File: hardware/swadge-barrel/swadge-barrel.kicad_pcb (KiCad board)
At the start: 2 copper layers, 70.4 x 89.6 mm, 46 parts, among them J1 USB_B_Micro, Q1 Q_NPN_BEC, SW1 SW_SPDT, U1 ESP-13-WROOM-02D, U2 OLED_DISPLAY, U3 BUS_PCIexpress, U4 QMA6981, U5 AP1117-33, U6 OLED_CONNECTOR

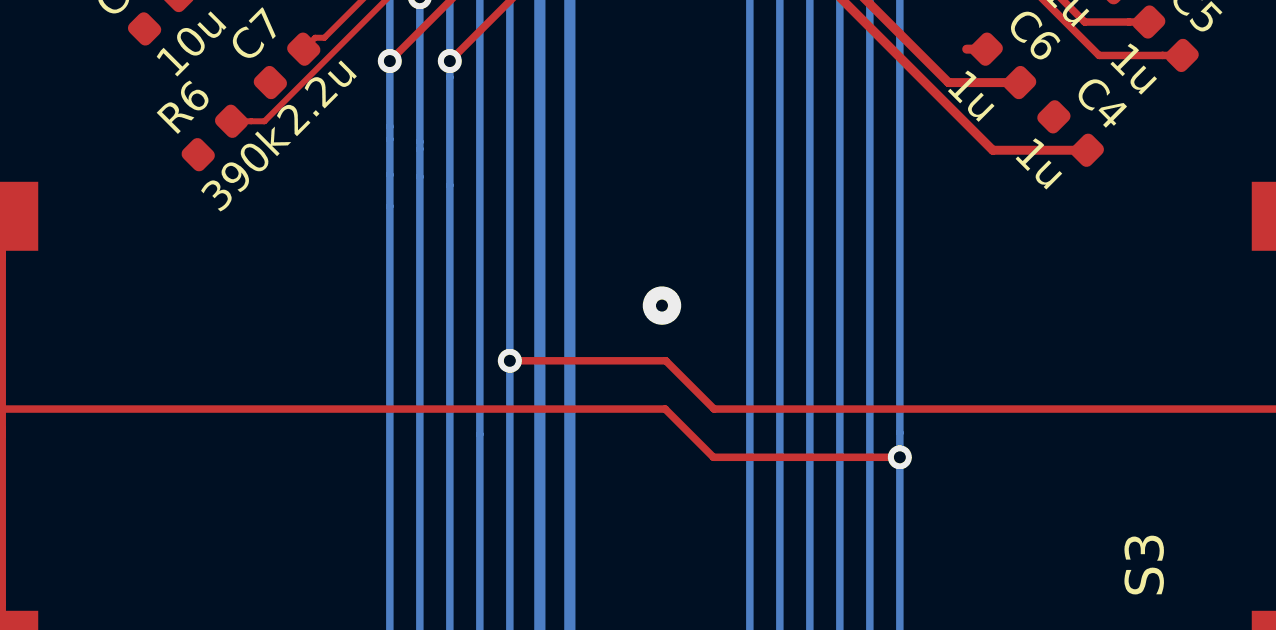
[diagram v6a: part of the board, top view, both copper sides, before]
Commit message: Added headband part and 3D model
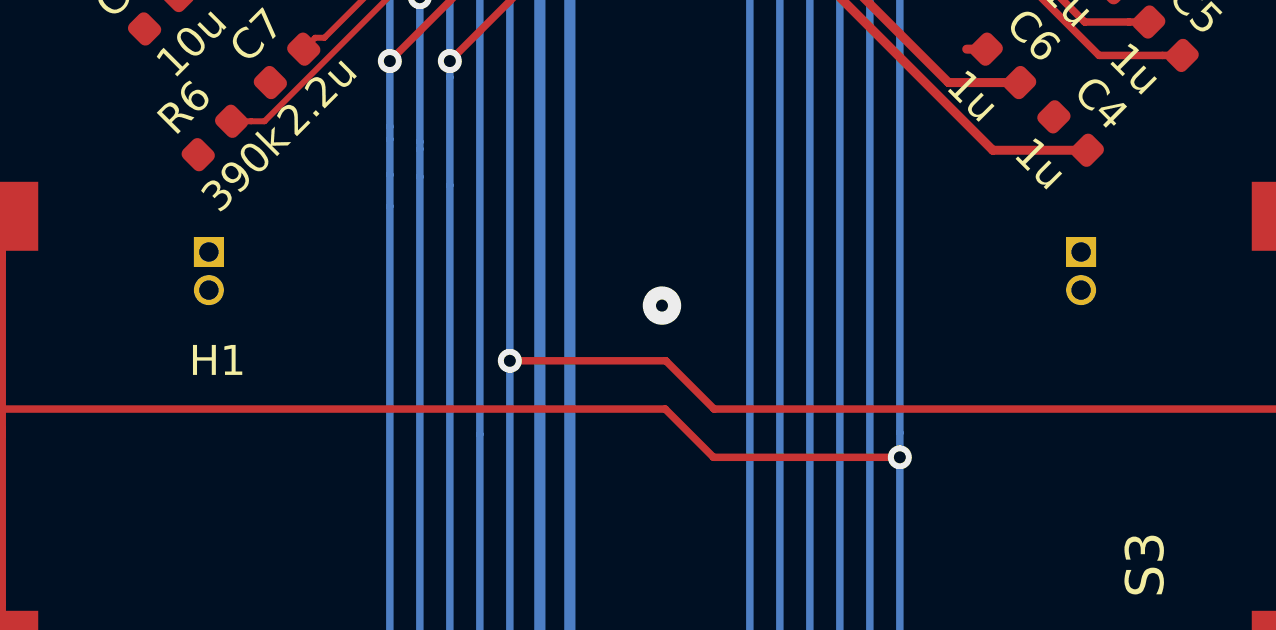
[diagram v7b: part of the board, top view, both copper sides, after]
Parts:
- added H1: Headband, Swadge_Parts:Headband, F.Cu at (145.5, 95.8)

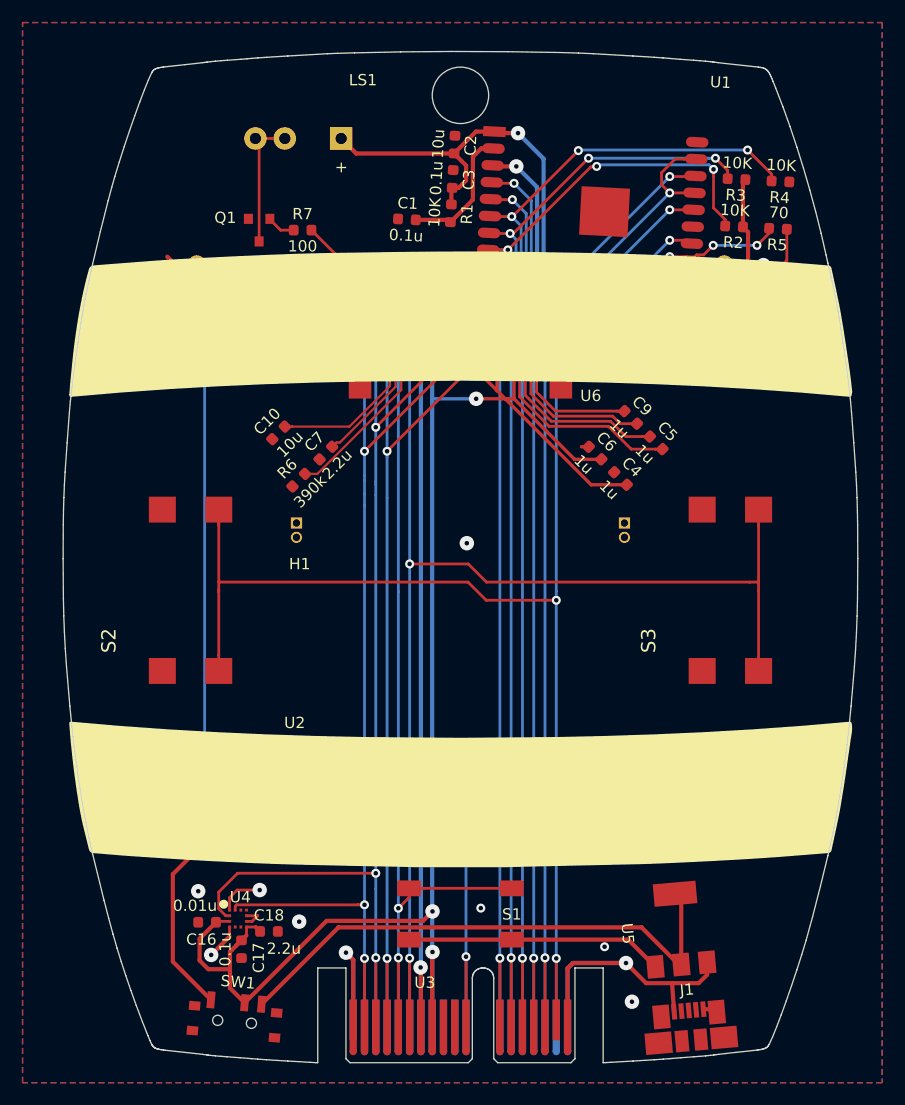
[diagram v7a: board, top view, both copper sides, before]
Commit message: Added vertical banding, shifted parts to avoid the bands
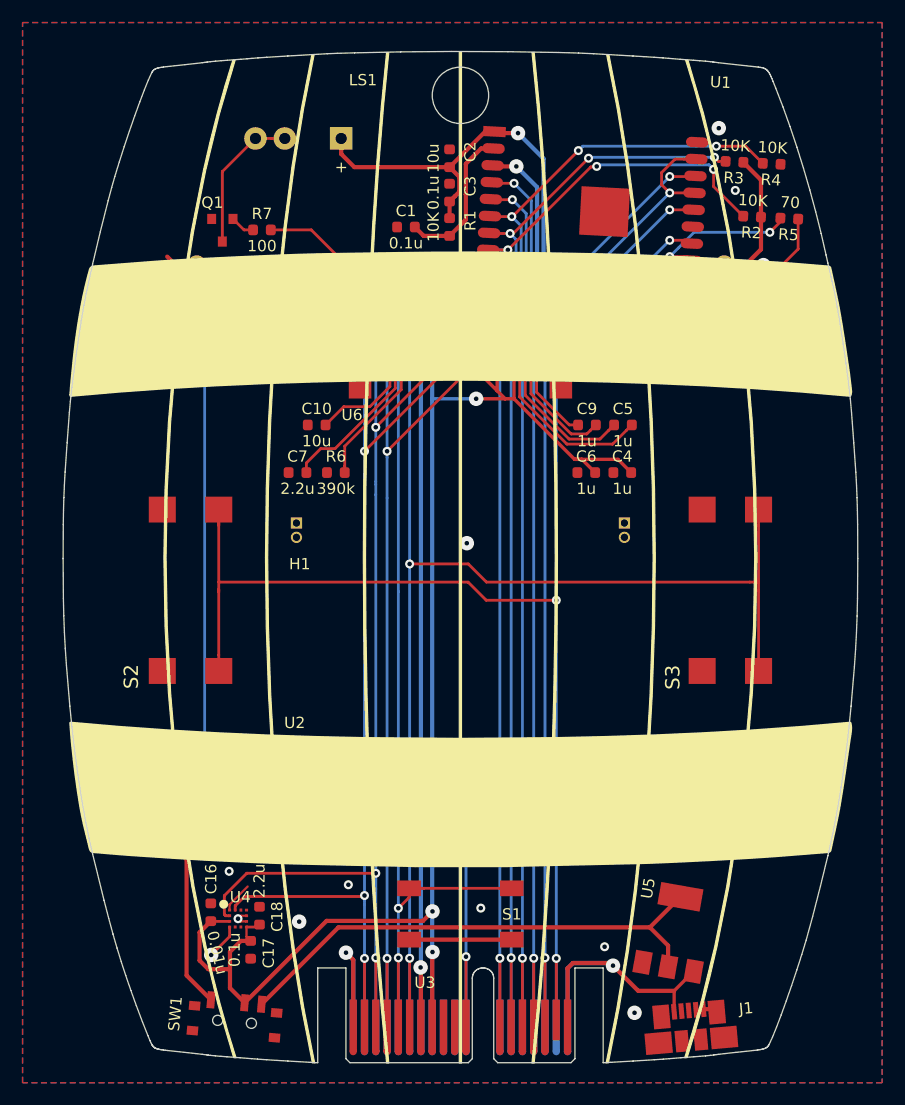
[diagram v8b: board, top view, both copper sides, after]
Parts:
- moved C9 3.94 mm to (156.7, 86.5), turned to 0 degrees
- moved R7 3.60 mm to (127.9, 69.2)
- moved C10 3.45 mm to (132.8, 86.5), turned to 0 degrees
- moved R6 3.36 mm to (134.5, 90.7), turned to 0 degrees
- moved C5 3.34 mm to (159.9, 86.5), turned to 0 degrees
- moved Q1 3.26 mm to (124.4, 69.2)
- moved C7 3.05 mm to (131.1, 90.7), turned to 0 degrees
- moved C6 1.90 mm to (156.7, 90.7), turned to 0 degrees
- moved R2 1.82 mm to (171.4, 68.0)
- moved R4 1.75 mm to (173.1, 63.3)
- moved C18 1.63 mm to (127.7, 130.0), turned to 90 degrees
- moved R3 1.54 mm to (169.8, 63.1)
- moved R5 1.35 mm to (174.6, 68.2)
- moved C2 1.29 mm to (144.5, 62.8), turned to 270 degrees
- moved C3 1.24 mm to (144.5, 65.9), turned to 270 degrees
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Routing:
- net GND: track 89.4 -> 73.3 mm, vias 11 -> 14
- net +3V3: track 314.1 -> 310.1 mm
- net Net-(C7-Pad2): track 10.6 -> 14.4 mm
- net Net-(C10-Pad2): track 13.5 -> 9.90 mm
- net BZR: track 113.3 -> 116.9 mm
- net Net-(C9-Pad1): track 11.8 -> 8.16 mm
- net +5V: track 32.8 -> 29.4 mm
- net RX: track 89.1 -> 92.2 mm, vias 4 -> 3
- net Net-(C9-Pad2): track 13.9 -> 11.0 mm
- net Net-(C5-Pad1): track 16.1 -> 13.5 mm
- net Net-(R6-Pad2): track 14.7 -> 12.5 mm
- net Net-(C5-Pad2): track 18.3 -> 16.1 mm
- net SDA: track 135.2 -> 133.1 mm
- net Net-(SW1-Pad3): track 47.9 -> 46.0 mm
- net Net-(LS1-Pad2): track 11.9 -> 13.4 mm
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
